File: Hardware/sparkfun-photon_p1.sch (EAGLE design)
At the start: 51 parts, among them U1 WM-N-BM-14

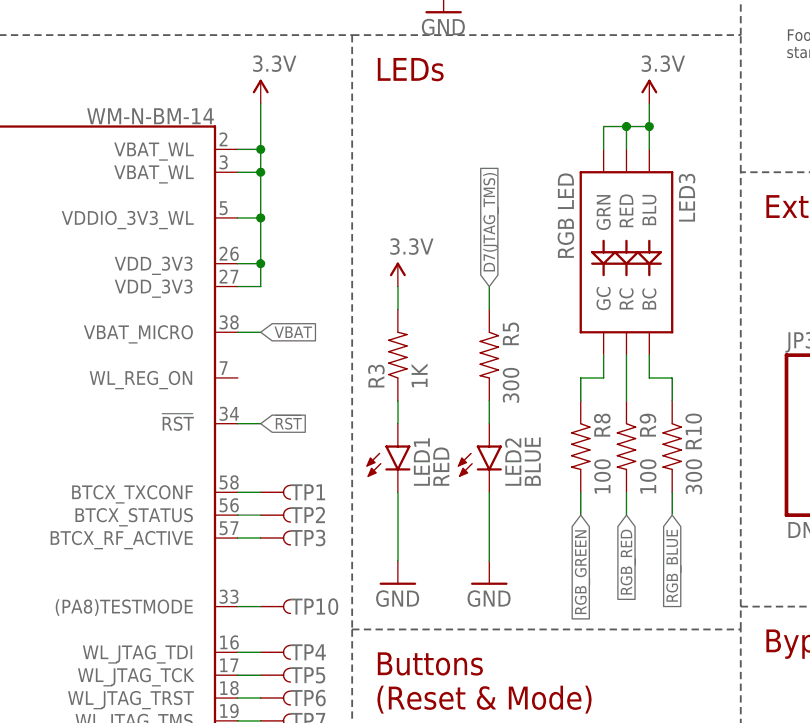
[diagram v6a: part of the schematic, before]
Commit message: Adding jumper to disconnect Power LED.
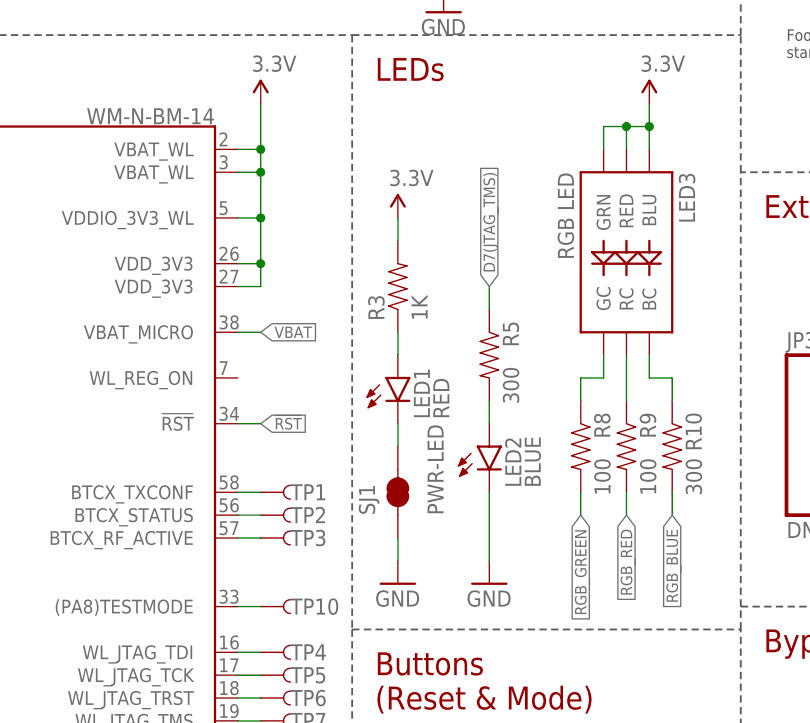
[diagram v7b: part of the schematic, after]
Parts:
- added SJ1: PWR-LED, SparkFun-Passives:JUMPER-PAD-2-NC_BY_TRACE
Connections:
- new net N$2: LED1.C, SJ1.2
- net GND: now also SJ1.1; no longer LED1.C
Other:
- moved on the sheet: LED1, R3
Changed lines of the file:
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@@
 <part name="TP9" library="SparkFun-Passives" deviceset="TEST-POINT" device="TP_15TH_THRU" value="TEST-POINTTP_15TH_THRU"/>
 <part name="TP10" library="SparkFun-Passives" deviceset="TEST-POINT" device="TP_15TH_THRU" value="TEST-POINTTP_15TH_THRU"/>
+<part name="SJ1" library="SparkFun-Passives" deviceset="JUMPER-PAD-2-NC_BY_TRACE" device="" value="PWR-LED"/>
 </parts>
 <sheets>
@@
 <attribute name="VALUE" x="120.904" y="105.41" size="1.778" layer="96" rot="R270"/>
 </instance>
-<instance part="LED1" gate="G$1" x="109.22" y="96.52"/>
-<instance part="R3" gate="G$1" x="109.22" y="106.68" rot="R90"/>
+<instance part="LED1" gate="G$1" x="109.22" y="104.14"/>
+<instance part="R3" gate="G$1" x="109.22" y="114.3" rot="R90"/>
 <instance part="GND6" gate="1" x="109.22" y="81.28"/>
 <instance part="GND14" gate="1" x="182.88" y="132.08"/>
@@
 </instance>
 <instance part="FRAME1" gate="V" x="147.32" y="0"/>
-<instance part="SUPPLY5" gate="G$1" x="109.22" y="114.3"/>
+<instance part="SUPPLY5" gate="G$1" x="109.22" y="121.92"/>
 <instance part="TP3" gate="G$1" x="93.98" y="86.36" smashed="yes">
 <attribute name="NAME" x="97.282" y="86.36" size="1.778" layer="95" align="center-left"/>
@@
 <attribute name="NAME" x="97.282" y="78.74" size="1.778" layer="95" align="center-left"/>
 </instance>
+<instance part="SJ1" gate="G$1" x="109.22" y="91.44" rot="R90"/>
 </instances>
 <busses>
@@
 <pinref part="GND9" gate="1" pin="GND"/>
 <wire x1="119.38" y1="91.44" x2="119.38" y2="83.82" width="0.1524" layer="91"/>
-</segment>
-<segment>
-<pinref part="GND6" gate="1" pin="GND"/>
-<pinref part="LED1" gate="G$1" pin="C"/>
-<wire x1="109.22" y1="83.82" x2="109.22" y2="91.44" width="0.1524" layer="91"/>
 </segment>
 <segment>
@@
 <pinref part="JP4" gate="G$1" pin="1"/>
 </segment>
+<segment>
+<pinref part="SJ1" gate="G$1" pin="1"/>
+<pinref part="GND6" gate="1" pin="GND"/>
+<wire x1="109.22" y1="86.36" x2="109.22" y2="83.82" width="0.1524" layer="91"/>
+</segment>
 </net>
 <net name="3.3V" class="0">
@@
 <pinref part="R3" gate="G$1" pin="2"/>
 <pinref part="SUPPLY5" gate="G$1" pin="3.3V"/>
-<wire x1="109.22" y1="114.3" x2="109.22" y2="111.76" width="0.1524" layer="91"/>
+<wire x1="109.22" y1="121.92" x2="109.22" y2="119.38" width="0.1524" layer="91"/>
 </segment>
 </net>
@@
 <pinref part="R3" gate="G$1" pin="1"/>
 <pinref part="LED1" gate="G$1" pin="A"/>
-<wire x1="109.22" y1="101.6" x2="109.22" y2="99.06" width="0.1524" layer="91"/>
+<wire x1="109.22" y1="109.22" x2="109.22" y2="106.68" width="0.1524" layer="91"/>
 </segment>
 </net>
@@
 </segment>
 </net>
+<net name="N$2" class="0">
+<segment>
+<pinref part="SJ1" gate="G$1" pin="2"/>
+<pinref part="LED1" gate="G$1" pin="C"/>
+<wire x1="109.22" y1="96.52" x2="109.22" y2="99.06" width="0.1524" layer="91"/>
+</segment>
+</net>

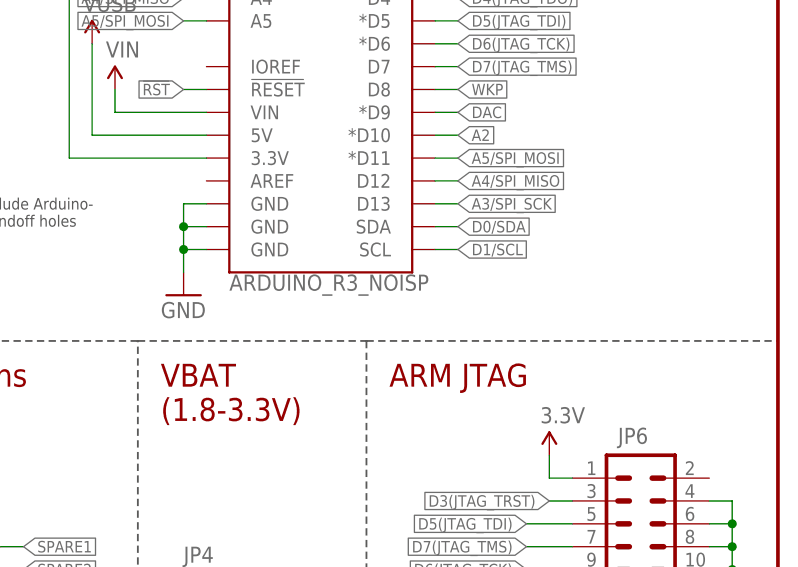
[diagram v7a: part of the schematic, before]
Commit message: Changing Arduino headers to locking footprints.
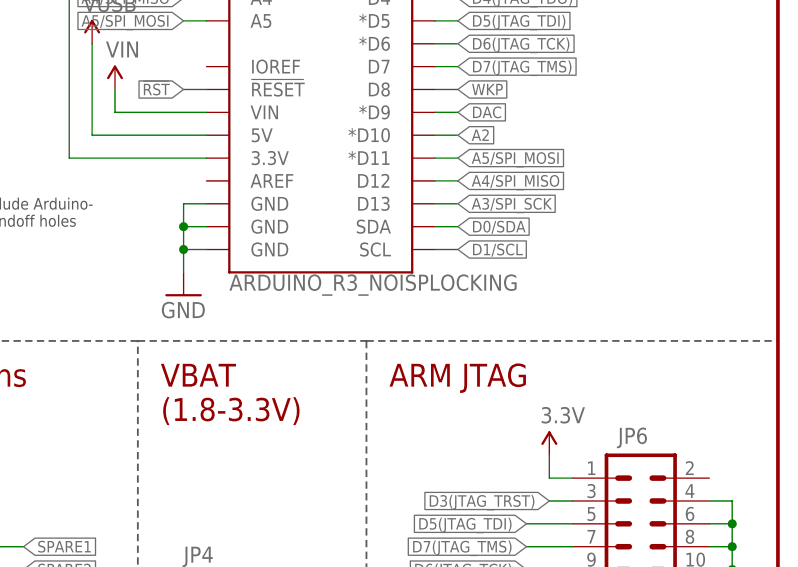
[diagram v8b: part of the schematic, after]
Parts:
- JP5: value ARDUINO_R3_NOISP -> ARDUINO_R3_NOISPLOCKING; device sparkfun_photon_temp:ARDUINO_R3_NOISP -> sparkfun_photon_temp:ARDUINO_R3_NOISPLOCKING
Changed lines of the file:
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@@
 <grid distance="0.1" unitdist="inch" unit="inch" style="lines" multiple="1" display="no" altdistance="0.01" altunitdist="inch" altunit="inch"/>
 <layers>
-<layer number="1" name="Top" color="4" fill="1" visible="no" active="no"/>
-<layer number="2" name="Route2" color="1" fill="3" visible="no" active="no"/>
-<layer number="3" name="Route3" color="4" fill="3" visible="no" active="no"/>
-<layer number="4" name="Route4" color="1" fill="4" visible="no" active="no"/>
-<layer number="5" name="Route5" color="4" fill="4" visible="no" active="no"/>
-<layer number="6" name="Route6" color="1" fill="8" visible="no" active="no"/>
-<layer number="7" name="Route7" color="4" fill="8" visible="no" active="no"/>
-<layer number="8" name="Route8" color="1" fill="2" visible="no" active="no"/>
-<layer number="9" name="Route9" color="4" fill="2" visible="no" active="no"/>
-<layer number="10" name="Route10" color="1" fill="7" visible="no" active="no"/>
-<layer number="11" name="Route11" color="4" fill="7" visible="no" active="no"/>
-<layer number="12" name="Route12" color="1" fill="5" visible="no" active="no"/>
-<layer number="13" name="Route13" color="4" fill="5" visible="no" active="no"/>
-<layer number="14" name="Route14" color="1" fill="6" visible="no" active="no"/>
-<layer number="15" name="Route15" color="4" fill="6" visible="no" active="no"/>
-<layer number="16" name="Bottom" color="1" fill="1" visible="no" active="no"/>
-<layer number="17" name="Pads" color="2" fill="1" visible="no" active="no"/>
-<layer number="18" name="Vias" color="2" fill="1" visible="no" active="no"/>
-<layer number="19" name="Unrouted" color="6" fill="1" visible="no" active="no"/>
-<layer number="20" name="Dimension" color="15" fill="1" visible="no" active="no"/>
-<layer number="21" name="tPlace" color="16" fill="1" visible="no" active="no"/>
-<layer number="22" name="bPlace" color="14" fill="1" visible="no" active="no"/>
-<layer number="23" name="tOrigins" color="15" fill="1" visible="no" active="no"/>
-<layer number="24" name="bOrigins" color="15" fill="1" visible="no" active="no"/>
-<layer number="25" name="tNames" color="7" fill="1" visible="no" active="no"/>
-<layer number="26" name="bNames" color="7" fill="1" visible="no" active="no"/>
-<layer number="27" name="tValues" color="7" fill="1" visible="no" active="no"/>
-<layer number="28" name="bValues" color="7" fill="1" visible="no" active="no"/>
+<layer number="1" name="Top" color="4" fill="1" visible="yes" active="no"/>
+<layer number="2" name="Route2" color="1" fill="3" visible="yes" active="no"/>
+<layer number="3" name="Route3" color="4" fill="3" visible="yes" active="no"/>
+<layer number="4" name="Route4" color="1" fill="4" visible="yes" active="no"/>
+<layer number="5" name="Route5" color="4" fill="4" visible="yes" active="no"/>
+<layer number="6" name="Route6" color="1" fill="8" visible="yes" active="no"/>
+<layer number="7" name="Route7" color="4" fill="8" visible="yes" active="no"/>
+<layer number="8" name="Route8" color="1" fill="2" visible="yes" active="no"/>
+<layer number="9" name="Route9" color="4" fill="2" visible="yes" active="no"/>
+<layer number="10" name="Route10" color="1" fill="7" visible="yes" active="no"/>
+<layer number="11" name="Route11" color="4" fill="7" visible="yes" active="no"/>
+<layer number="12" name="Route12" color="1" fill="5" visible="yes" active="no"/>
+<layer number="13" name="Route13" color="4" fill="5" visible="yes" active="no"/>
+<layer number="14" name="Route14" color="1" fill="6" visible="yes" active="no"/>
+<layer number="15" name="Route15" color="4" fill="6" visible="yes" active="no"/>
+<layer number="16" name="Bottom" color="1" fill="1" visible="yes" active="no"/>
+<layer number="17" name="Pads" color="2" fill="1" visible="yes" active="no"/>
+<layer number="18" name="Vias" color="2" fill="1" visible="yes" active="no"/>
+<layer number="19" name="Unrouted" color="6" fill="1" visible="yes" active="no"/>
+<layer number="20" name="Dimension" color="15" fill="1" visible="yes" active="no"/>
+<layer number="21" name="tPlace" color="16" fill="1" visible="yes" active="no"/>
+<layer number="22" name="bPlace" color="14" fill="1" visible="yes" active="no"/>
+<layer number="23" name="tOrigins" color="15" fill="1" visible="yes" active="no"/>
+<layer number="24" name="bOrigins" color="15" fill="1" visible="yes" active="no"/>
+<layer number="25" name="tNames" color="7" fill="1" visible="yes" active="no"/>
+<layer number="26" name="bNames" color="7" fill="1" visible="yes" active="no"/>
+<layer number="27" name="tValues" color="7" fill="1" visible="yes" active="no"/>
+<layer number="28" name="bValues" color="7" fill="1" visible="yes" active="no"/>
 <layer number="29" name="tStop" color="7" fill="3" visible="no" active="no"/>
 <layer number="30" name="bStop" color="7" fill="6" visible="no" active="no"/>
@@
 <layer number="35" name="tGlue" color="7" fill="4" visible="no" active="no"/>
 <layer number="36" name="bGlue" color="7" fill="5" visible="no" active="no"/>
-<layer number="37" name="tTest" color="7" fill="1" visible="no" active="no"/>
-<layer number="38" name="bTest" color="7" fill="1" visible="no" active="no"/>
+<layer number="37" name="tTest" color="7" fill="1" visible="yes" active="no"/>
+<layer number="38" name="bTest" color="7" fill="1" visible="yes" active="no"/>
 <layer number="39" name="tKeepout" color="4" fill="11" visible="no" active="no"/>
 <layer number="40" name="bKeepout" color="1" fill="11" visible="no" active="no"/>
@@
 <layer number="44" name="Drills" color="7" fill="1" visible="no" active="no"/>
 <layer number="45" name="Holes" color="7" fill="1" visible="no" active="no"/>
-<layer number="46" name="Milling" color="3" fill="1" visible="no" active="no"/>
-<layer number="47" name="Measures" color="7" fill="1" visible="no" active="no"/>
-<layer number="48" name="Document" color="7" fill="1" visible="no" active="no"/>
-<layer number="49" name="Reference" color="7" fill="1" visible="no" active="no"/>
-<layer number="50" name="dxf" color="7" fill="1" visible="no" active="no"/>
-<layer number="51" name="tDocu" color="6" fill="1" visible="no" active="no"/>
-<layer number="52" name="bDocu" color="7" fill="1" visible="no" active="no"/>
-<layer number="53" name="tGND_GNDA" color="7" fill="9" visible="no" active="no"/>
-<layer number="54" name="bGND_GNDA" color="1" fill="9" visible="no" active="no"/>
-<layer number="56" name="wert" color="7" fill="1" visible="no" active="no"/>
-<layer number="57" name="tCAD" color="7" fill="1" visible="no" active="no"/>
-<layer number="59" name="tCarbon" color="7" fill="1" visible="no" active="no"/>
-<layer number="60" name="bCarbon" color="7" fill="1" visible="no" active="no"/>
+<layer number="46" name="Milling" color="3" fill="1" visible="yes" active="no"/>
+<layer number="47" name="Measures" color="7" fill="1" visible="yes" active="no"/>
+<layer number="48" name="Document" color="7" fill="1" visible="yes" active="no"/>
+<layer number="49" name="Reference" color="7" fill="1" visible="yes" active="no"/>
+<layer number="50" name="dxf" color="7" fill="1" visible="yes" active="no"/>
+<layer number="51" name="tDocu" color="6" fill="1" visible="yes" active="no"/>
+<layer number="52" name="bDocu" color="7" fill="1" visible="yes" active="no"/>
+<layer number="53" name="tGND_GNDA" color="7" fill="9" visible="yes" active="no"/>
+<layer number="54" name="bGND_GNDA" color="1" fill="9" visible="yes" active="no"/>
+<layer number="56" name="wert" color="7" fill="1" visible="yes" active="no"/>
+<layer number="57" name="tCAD" color="7" fill="1" visible="yes" active="no"/>
+<layer number="59" name="tCarbon" color="7" fill="1" visible="yes" active="no"/>
+<layer number="60" name="bCarbon" color="7" fill="1" visible="yes" active="no"/>
 <layer number="90" name="Modules" color="5" fill="1" visible="yes" active="yes"/>
 <layer number="91" name="Nets" color="2" fill="1" visible="yes" active="yes"/>
@@
 <part name="SUPPLY11" library="SparkFun-Aesthetics" deviceset="VIN" device=""/>
 <part name="SUPPLY9" library="SparkFun-Aesthetics" deviceset="3.3V" device=""/>
-<part name="JP5" library="sparkfun_photon_temp" deviceset="ARDUINO_R3_NOISP" device=""/>
+<part name="JP5" library="sparkfun_photon_temp" deviceset="ARDUINO_R3_NOISP" device="LOCKING" value="ARDUINO_R3_NOISPLOCKING"/>
 <part name="C5" library="SparkFun-Capacitors" deviceset="10UF-6.3V-20%(0603)" device="" value="10uF"/>
 <part name="C7" library="SparkFun-Capacitors" deviceset="10UF-6.3V-20%(0603)" device="" value="10uF"/>
